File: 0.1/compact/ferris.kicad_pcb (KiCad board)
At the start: 2 copper layers, 208.7 x 86.7 mm, 102 parts, among them J1 USB C, K0_0 KEYSW, K0_1 KEYSW, K0_2 KEYSW, K0_3 KEYSW, K0_4 KEYSW, K0_5 KEYSW, K0_6 KEYSW, K0_7 KEYSW, K0_8 KEYSW, K0_9 KEYSW, K1_0 KEYSW, K1_1 KEYSW, K1_2 KEYSW, K1_3 KEYSW, K1_4 KEYSW, K1_5 KEYSW, K1_6 KEYSW, K1_7 KEYSW, K1_8 KEYSW, K1_9 KEYSW, K2_0 KEYSW, K2_1 KEYSW, K2_2 KEYSW, K2_3 KEYSW, K2_4 KEYSW, K2_5 KEYSW, K2_6 KEYSW, K2_7 KEYSW, K2_8 KEYSW, K2_9 KEYSW, K3_3 KEYSW, K3_4 KEYSW, K3_5 KEYSW, K3_6 KEYSW, SW1 SW_PUSH, U1 ATmega32U4-AU, U2 MCP23017_SO, Y1 Crystal

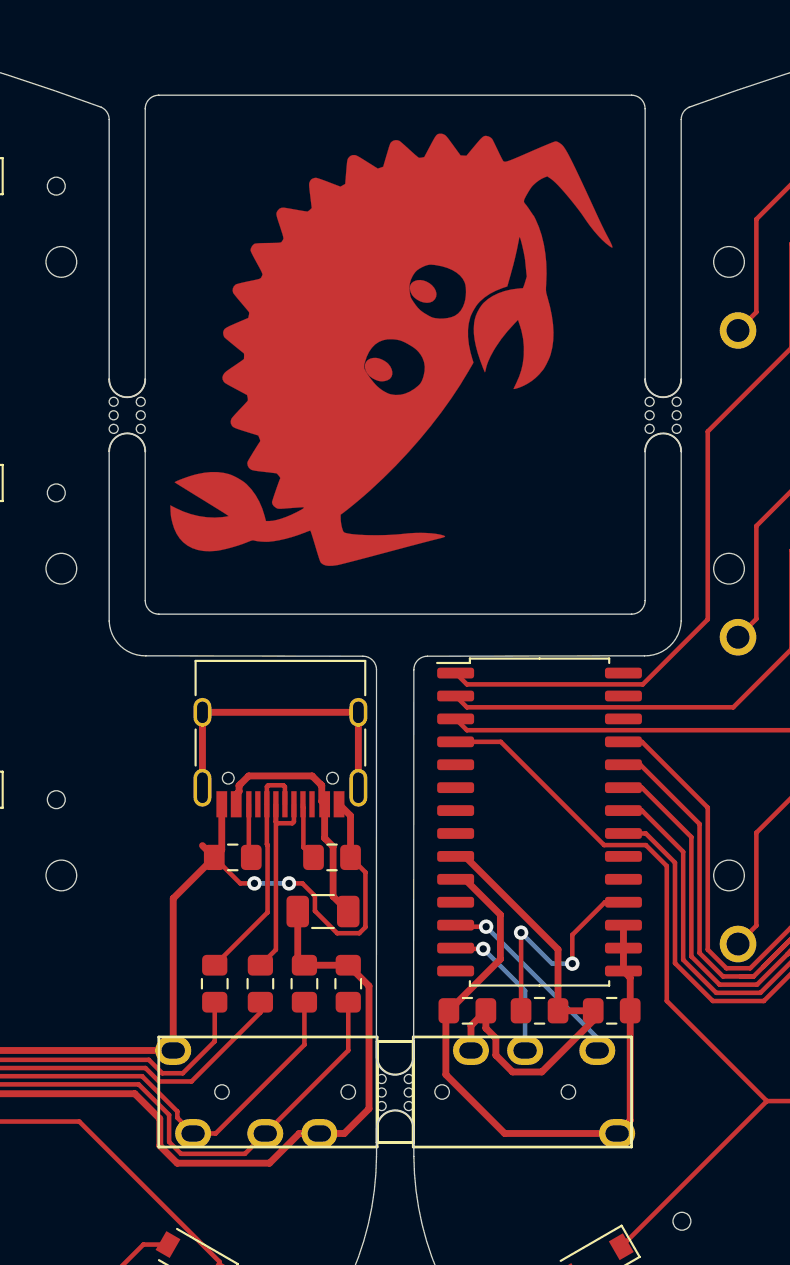
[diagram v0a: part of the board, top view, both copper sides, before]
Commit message: Make all mouse bites 5mm.
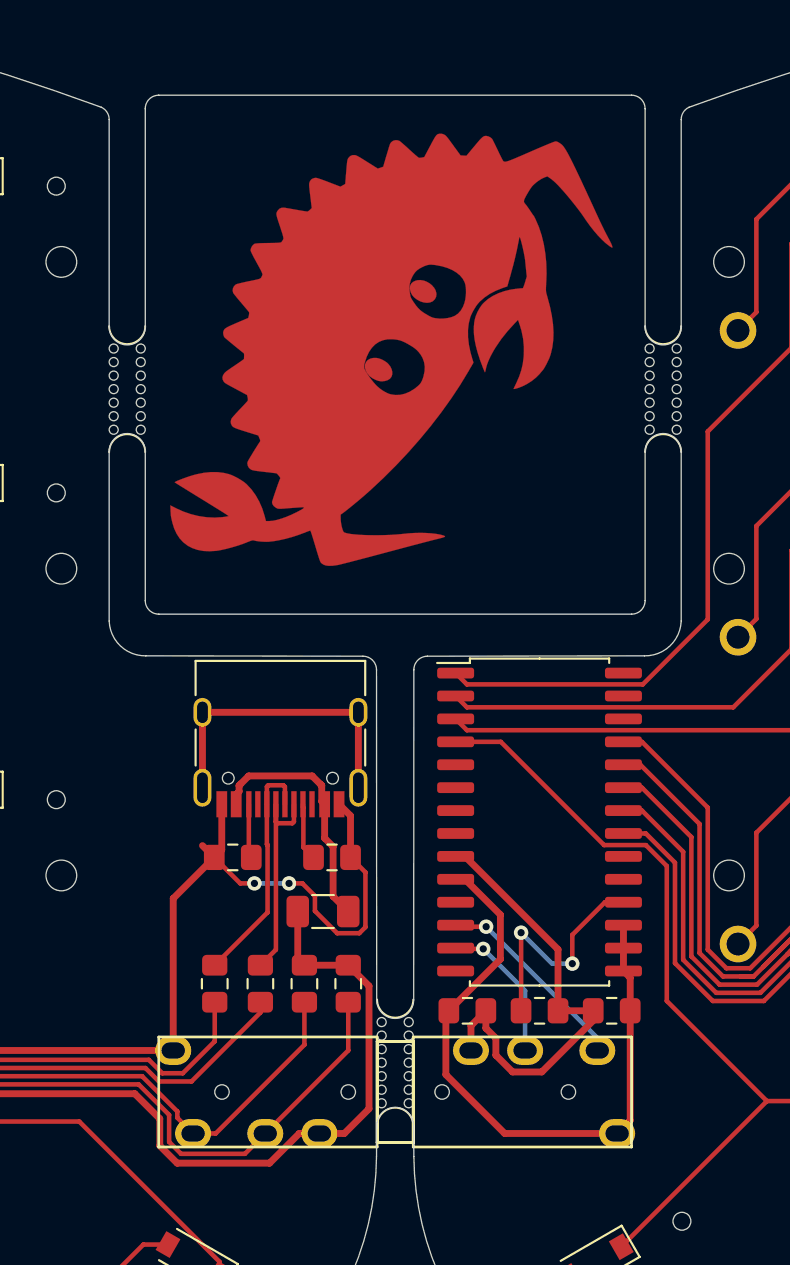
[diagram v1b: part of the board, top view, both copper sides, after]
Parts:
- removed mouse-bite-2mm-slot (x3): VAL**, panelization:mouse-bite-2mm-slot
- added mouse-bite-5mm-slot: VAL**, panelization:mouse-bite-5mm-slot, F.Cu at (103.2, 35.5)
- added mouse-bite-5mm-slot: VAL**, panelization:mouse-bite-5mm-slot, F.Cu at (118.0, 75.9)
- added mouse-bite-5mm-slot: VAL**, panelization:mouse-bite-5mm-slot, F.Cu at (132.8, 38.5)
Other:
- outline, holes or cut-outs redrawn

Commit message: Add JLCPCB order number placeholder.
Also, make the text on the scrap panel concise.
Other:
- board text added: "Ferris Compact - v0.1 by @pierrec83 Fully open source design: github.com/pierrechevalier83/ferris Fab by JLCPCB: JLCJLCJLCJLC"
- board text removed: "Ferris Compact - v0.1 by @pierrec83 A keyboard with only the features you need :) * Split, 34 Keys * Kailh Choc footprints: pg1350 * Choc spacing: 17x18mm * Microcontroller: Atmega32u4 * IO Expander: MCP23017 * USB C * Dimensions: 209x98mm Fully open source design: github.com/pierrechevalier83/ferris"
